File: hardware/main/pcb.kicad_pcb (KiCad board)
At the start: 2 copper layers, 42 x 42 mm, 13 parts, among them J3 Conn_01x03_Socket

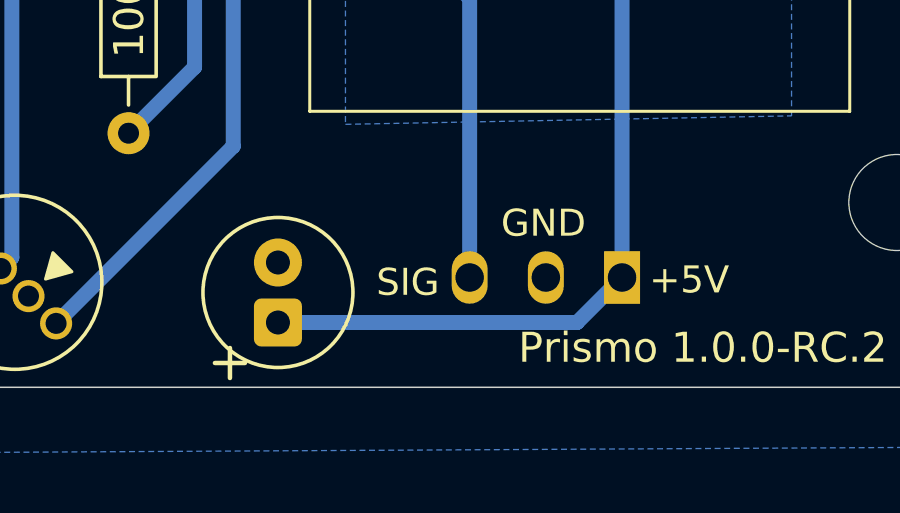
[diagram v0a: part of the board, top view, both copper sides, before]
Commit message: add the Capacitors for 5V and 3.3V
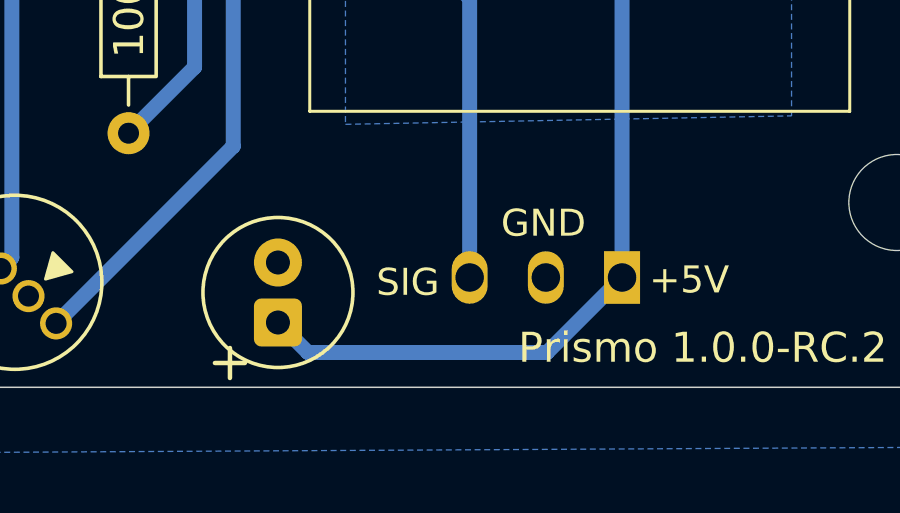
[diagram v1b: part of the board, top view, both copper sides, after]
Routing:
- net +5V: track 157.2 -> 158.0 mm
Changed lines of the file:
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@@
+	)
+	(segment
+		(start 128.34 86.5)
+		(end 130.84 84)
+		(width 0.5)
+		(layer "B.Cu")
+		(net "+5V")
+	)
+	(segment
+		(start 119.37 85.5)
+		(end 120.37 86.5)
+		(width 0.5)
+		(layer "B.Cu")
+		(net "+5V")
 	)
 	(segment
@@
 		(start 144.3 83.785)
 		(end 144.3 49.96)
-		(width 0.5)
-		(layer "B.Cu")
-		(net "+5V")
-	)
-	(segment
-		(start 129.34 85.5)
-		(end 130.84 84)
 		(width 0.5)
 		(layer "B.Cu")
@@
 	)
 	(segment
+		(start 120.37 86.5)
+		(end 128.34 86.5)
+		(width 0.5)
+		(layer "B.Cu")
+		(net "+5V")
+	)
+	(segment
 		(start 144.3 49.96)
 		(end 144.29 49.95)
@@
 		(width 0.5)
 		(layer "B.Cu")
-		(net "+5V")
-	)
-	(segment
-		(start 119.37 85.5)
-		(end 129.34 85.5)
-		(width 0.5)
-		(layer "B.Cu")

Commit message: add capasitors to led
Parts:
- added C3: 100nF, prismo:C_Disc_D3.0mm_W1.6mm_P2.50mm, F.Cu at (111.8, 77.5)
- added C4: 100nF, prismo:C_Disc_D3.0mm_W1.6mm_P2.50mm, F.Cu at (119.2, 50.5)
- added C5: 100nF, prismo:C_Disc_D3.0mm_W1.6mm_P2.50mm, F.Cu at (144.6, 53.3)
- added C6: 100nF, prismo:C_Disc_D3.0mm_W1.6mm_P2.50mm, F.Cu at (144.6, 80.0)
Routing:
- net +5V: track 158.0 -> 162.8 mm

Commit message: small reroute
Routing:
- net +5V: track 162.8 -> 159.9 mm
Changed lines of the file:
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@@
+	)
+	(segment
+		(start 137.05 55.6)
+		(end 130.84 61.81)
+		(width 0.5)
+		(layer "B.Cu")
+		(net "+5V")
 	)
 	(segment
@@
 	)
 	(segment
+		(start 137.05 50.3)
+		(end 137.4 49.95)
+		(width 0.5)
+		(layer "B.Cu")
+		(net "+5V")
+	)
+	(segment
 		(start 128.34 86.5)
 		(end 130.84 84)
@@
 	)
 	(segment
-		(start 130.84 84)
-		(end 130.84 49.95)
-		(width 0.5)
-		(layer "B.Cu")
-		(net "+5V")
-	)
-	(segment
-		(start 137.4 55.6)
-		(end 137.4 49.95)
+		(start 130.84 61.81)
+		(end 130.84 84)
 		(width 0.5)
 		(layer "B.Cu")
@@
 		(start 137.4 49.95)
 		(end 130.84 49.95)
+		(width 0.5)
+		(layer "B.Cu")
+		(net "+5V")
+	)
+	(segment
+		(start 137.05 55.6)
+		(end 137.05 50.3)
 		(width 0.5)
 		(layer "B.Cu")
@@
 		(polygon
 			(pts
-				(xy 121.62 78.894431) (xy 136.49 78.612089) (xy 136.49 53.66) (xy 121.62 53.66)
+				(xy 121.699928 78.87) (xy 136.599912 78.81) (xy 136.49 53.66) (xy 121.61 53.72)
 			)
 		)
